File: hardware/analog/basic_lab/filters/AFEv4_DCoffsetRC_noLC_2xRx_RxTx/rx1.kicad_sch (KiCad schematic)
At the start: 7 parts

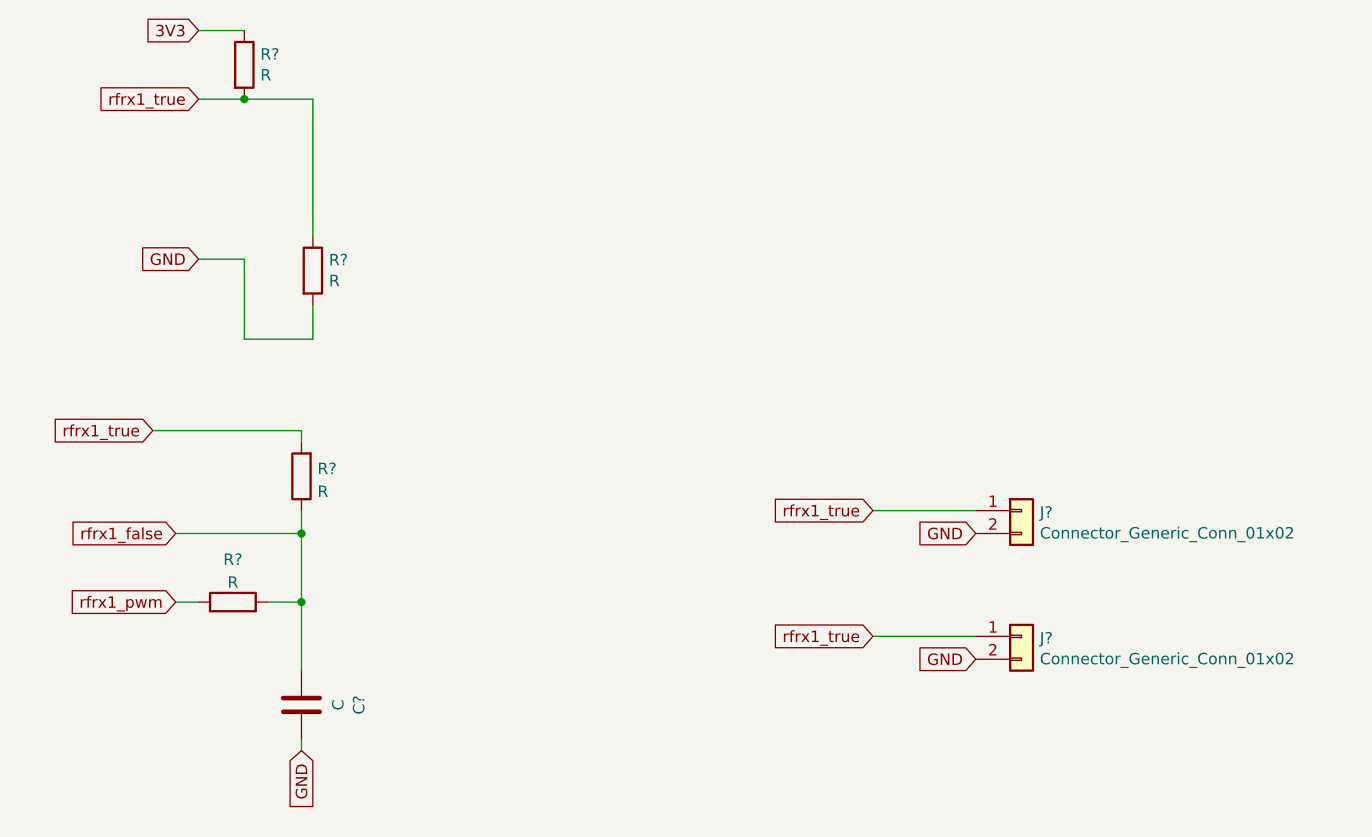
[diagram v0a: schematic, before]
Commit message: started 2xRx / RxTx PCBs with no / simple LC filters
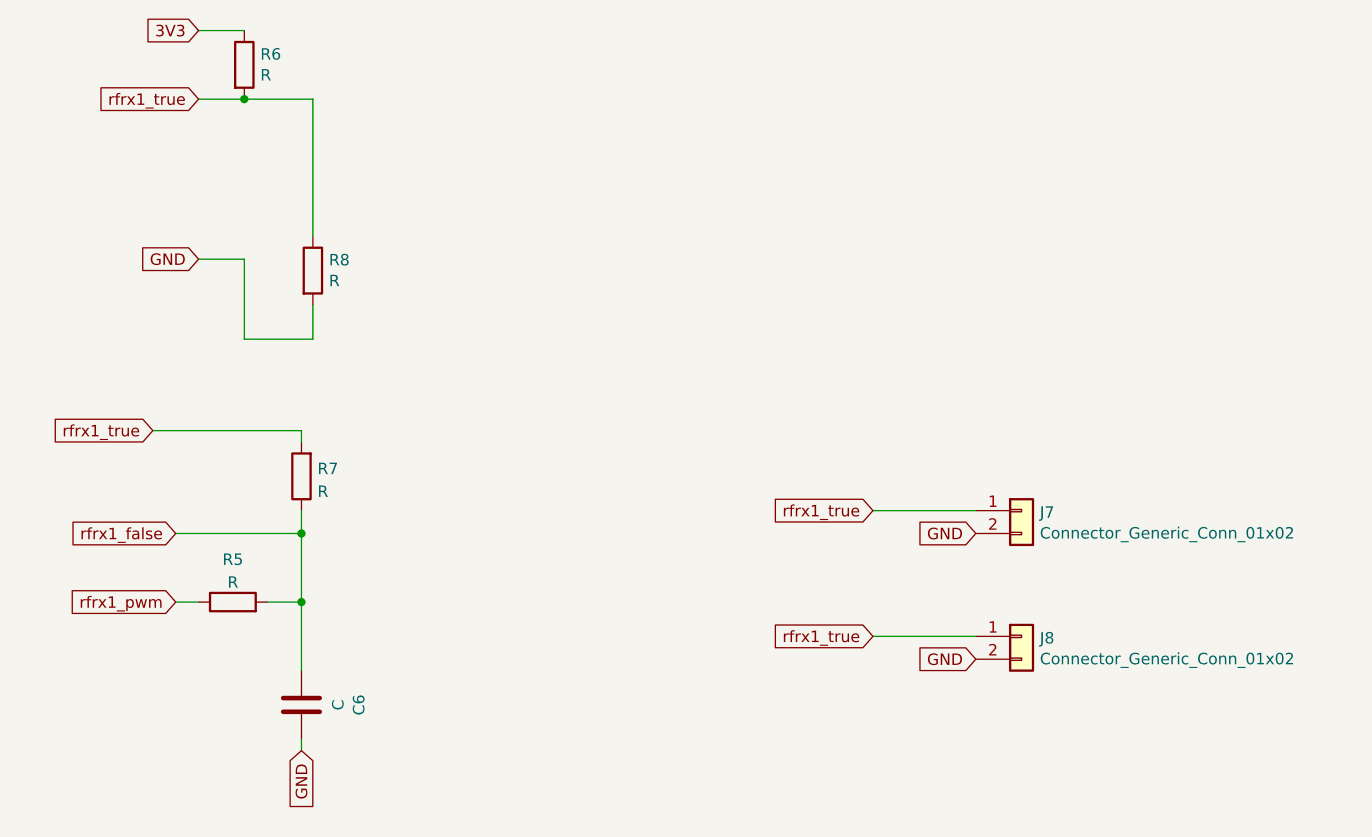
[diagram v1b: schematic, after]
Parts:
- gave numbers to parts that had none: 7
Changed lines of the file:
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@@
   (symbol (lib_id "Device:R") (at 87.63 96.52 180) (unit 1)
     (in_bom yes) (on_board yes) (fields_autoplaced)
-    (property "Reference" "R?" (id 0) (at 89.408 95.6853 0)
+    (property "Reference" "R7" (id 0) (at 89.408 95.6853 0)
       (effects (font (size 1.27 1.27)) (justify right))
     )
@@
   (symbol (lib_id "Device:C") (at 87.63 121.92 180) (unit 1)
     (in_bom yes) (on_board yes)
-    (property "Reference" "C?" (id 0) (at 94.0308 121.92 90))
+    (property "Reference" "C6" (id 0) (at 94.0308 121.92 90))
     (property "Value" "C" (id 1) (at 91.7194 121.92 90))
     (property "Footprint" "Capacitor_THT:C_Axial_L3.8mm_D2.6mm_P7.50mm_Horizontal" (id 2) (at 86.6648 118.11 0)
@@
   (symbol (lib_id "Device:R") (at 88.9 73.66 0) (unit 1)
     (in_bom yes) (on_board yes)
-    (property "Reference" "R?" (id 0) (at 90.678 72.4916 0)
+    (property "Reference" "R8" (id 0) (at 90.678 72.4916 0)
       (effects (font (size 1.27 1.27)) (justify left))
     )
@@
   (symbol (lib_id "bgt:Connector_Generic_Conn_01x02") (at 167.64 114.3 0) (unit 1)
     (in_bom yes) (on_board yes)
-    (property "Reference" "J?" (id 0) (at 169.672 114.5032 0)
+    (property "Reference" "J8" (id 0) (at 169.672 114.5032 0)
       (effects (font (size 1.27 1.27)) (justify left))
     )
@@
   (symbol (lib_id "Device:R") (at 80.01 110.49 90) (unit 1)
     (in_bom yes) (on_board yes) (fields_autoplaced)
-    (property "Reference" "R?" (id 0) (at 80.01 105.7742 90))
+    (property "Reference" "R5" (id 0) (at 80.01 105.7742 90))
     (property "Value" "R" (id 1) (at 80.01 108.3111 90))
     (property "Footprint" "Resistor_THT:R_Axial_DIN0207_L6.3mm_D2.5mm_P5.08mm_Vertical" (id 2) (at 80.01 112.268 90)
@@
   (symbol (lib_id "bgt:Connector_Generic_Conn_01x02") (at 167.64 100.33 0) (unit 1)
     (in_bom yes) (on_board yes)
-    (property "Reference" "J?" (id 0) (at 169.672 100.5332 0)
+    (property "Reference" "J7" (id 0) (at 169.672 100.5332 0)
       (effects (font (size 1.27 1.27)) (justify left))
     )
@@
   (symbol (lib_id "Device:R") (at 81.28 50.8 0) (unit 1)
     (in_bom yes) (on_board yes)
-    (property "Reference" "R?" (id 0) (at 83.058 49.6316 0)
+    (property "Reference" "R6" (id 0) (at 83.058 49.6316 0)
       (effects (font (size 1.27 1.27)) (justify left))
     )

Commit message: started 2xRx / RxTx PCBs with no / simple LC filters: Gerber with THT board; started SMD board in the same DIR
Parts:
- C6: footprint Capacitor_THT:C_Axial_L3.8mm_D2.6mm_P7.50mm_Horizontal -> Capacitor_SMD:C_1206_3216Metric
- R5, R6, R7, R8: footprint Resistor_THT:R_Axial_DIN0207_L6.3mm_D2.5mm_P5.08mm_Vertical -> Resistor_SMD:R_1206_3216Metric
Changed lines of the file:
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@@
       (effects (font (size 1.27 1.27)) (justify right))
     )
-    (property "Footprint" "Resistor_THT:R_Axial_DIN0207_L6.3mm_D2.5mm_P5.08mm_Vertical" (id 2) (at 89.408 96.52 90)
+    (property "Footprint" "Resistor_SMD:R_1206_3216Metric" (id 2) (at 89.408 96.52 90)
       (effects (font (size 1.27 1.27)) hide)
     )
@@
     (property "Reference" "C6" (id 0) (at 94.0308 121.92 90))
     (property "Value" "C" (id 1) (at 91.7194 121.92 90))
-    (property "Footprint" "Capacitor_THT:C_Axial_L3.8mm_D2.6mm_P7.50mm_Horizontal" (id 2) (at 86.6648 118.11 0)
+    (property "Footprint" "Capacitor_SMD:C_1206_3216Metric" (id 2) (at 86.6648 118.11 0)
       (effects (font (size 1.27 1.27)) hide)
     )
@@
       (effects (font (size 1.27 1.27)) (justify left))
     )
-    (property "Footprint" "Resistor_THT:R_Axial_DIN0207_L6.3mm_D2.5mm_P5.08mm_Vertical" (id 2) (at 87.122 73.66 90)
+    (property "Footprint" "Resistor_SMD:R_1206_3216Metric" (id 2) (at 87.122 73.66 90)
       (effects (font (size 1.27 1.27)) hide)
     )
@@
     (property "Reference" "R5" (id 0) (at 80.01 105.7742 90))
     (property "Value" "R" (id 1) (at 80.01 108.3111 90))
-    (property "Footprint" "Resistor_THT:R_Axial_DIN0207_L6.3mm_D2.5mm_P5.08mm_Vertical" (id 2) (at 80.01 112.268 90)
+    (property "Footprint" "Resistor_SMD:R_1206_3216Metric" (id 2) (at 80.01 112.268 90)
       (effects (font (size 1.27 1.27)) hide)
     )
@@
       (effects (font (size 1.27 1.27)) (justify left))
     )
-    (property "Footprint" "Resistor_THT:R_Axial_DIN0207_L6.3mm_D2.5mm_P5.08mm_Vertical" (id 2) (at 79.502 50.8 90)
+    (property "Footprint" "Resistor_SMD:R_1206_3216Metric" (id 2) (at 79.502 50.8 90)
       (effects (font (size 1.27 1.27)) hide)
     )

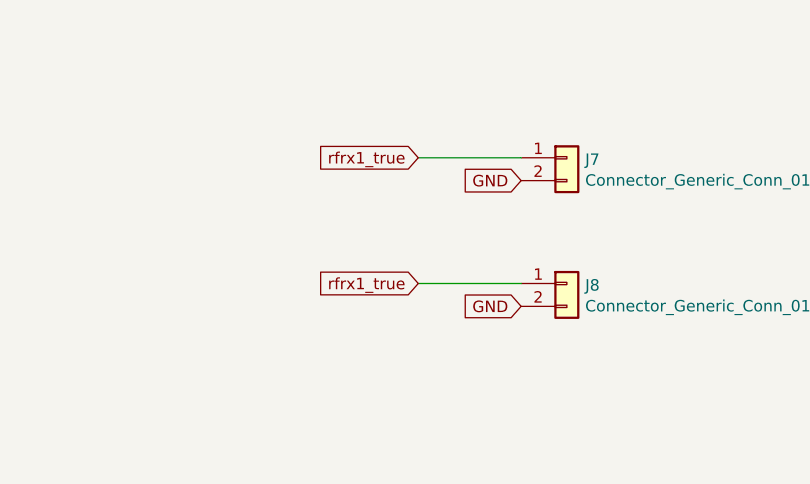
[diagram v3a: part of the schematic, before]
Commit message: started PCB LPF LC SMD: support by the main AFE brd
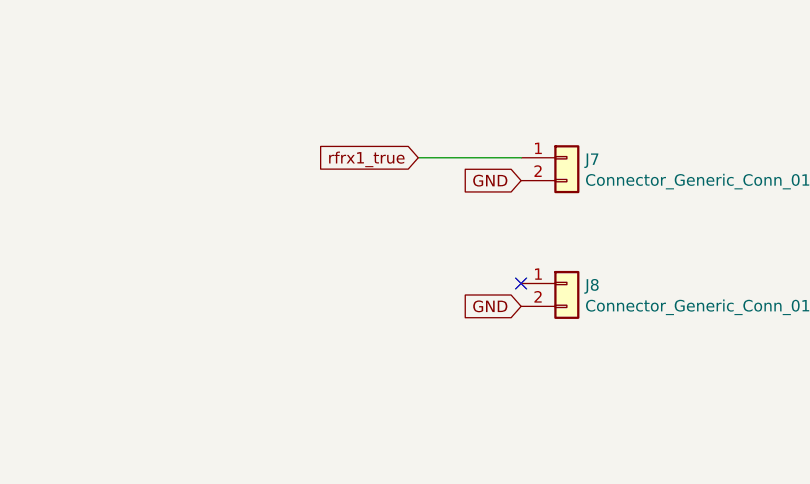
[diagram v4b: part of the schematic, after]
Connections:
- net rfrx1_true: no longer J8.1 (Pin_1)
- no-connect marks 0 -> 1
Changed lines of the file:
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@@
   (junction (at 87.63 102.87) (diameter 0) (color 0 0 0 0)
   )
+  (no_connect (at 162.56 114.3))
   (wire (pts (xy 81.28 72.39) (xy 81.28 81.28))
     (stroke (width 0) (type default) (color 0 0 0 0))
   )
   (wire (pts (xy 81.28 54.61) (xy 88.9 54.61))
-    (stroke (width 0) (type default) (color 0 0 0 0))
-  )
-  (wire (pts (xy 151.13 114.3) (xy 162.56 114.3))
     (stroke (width 0) (type default) (color 0 0 0 0))
   )
@@
     )
   )
-  (global_label "rfrx1_true" (shape input) (at 151.13 114.3 180) (fields_autoplaced)
-    (effects (font (size 1.27 1.27)) (justify right))
-    (property "Intersheet References" "${INTERSHEET_REFS}" (id 0) (at 139.5529 114.2206 0)
-      (effects (font (size 1.27 1.27)) (justify right) hide)
-    )
-  )
